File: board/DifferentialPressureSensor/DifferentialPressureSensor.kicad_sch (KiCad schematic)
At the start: 15 parts, among them U1 ESP32-S3-DEVKIT-LIPO

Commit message: -Enhance Datalogger Functionality and Update Rotary Encoder Configuration - Updated the datalogger_task to initialize sensor readings after resuming from sleep, ensuring fresh data is captured. - Changed the rotary encoder button pin from GPIO_NUM_7 to GPIO_NUM_2 - Adjusted inactivity timeout and sleep duration for better power management. - Added a callback for long button presses on the rotary encoder to enhance user interaction. - updated kicad design
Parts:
- R4: value 10k -> 4.7k
- R5: value 2k -> 4.7k
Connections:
- net +3.3V: now also Jrotary1.2 (Pin_2); no longer Jrotary1.1 (Pin_1)
- net GND: now also Jrotary1.1 (Pin_1); no longer Jrotary1.2 (Pin_2)
- net at U1.J3_2 (U0TXD/GPIO43): no longer Jrotary1.3 (Pin_3)
- net at U1.J3_5 (GPIO2): now also Jrotary1.3 (Pin_3)
- net at U1.J3_6 (GPIO42): now also Jrotary1.5 (Pin_5); no longer Jrotary1.4 (Pin_4)
- net at U1.J3_7 (GPIO41): now also Jrotary1.4 (Pin_4); no longer Jrotary1.5 (Pin_5)
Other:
- moved on the sheet: Ji2c1, Ji2c2, Ji2c3, Joled1, Jrotary1

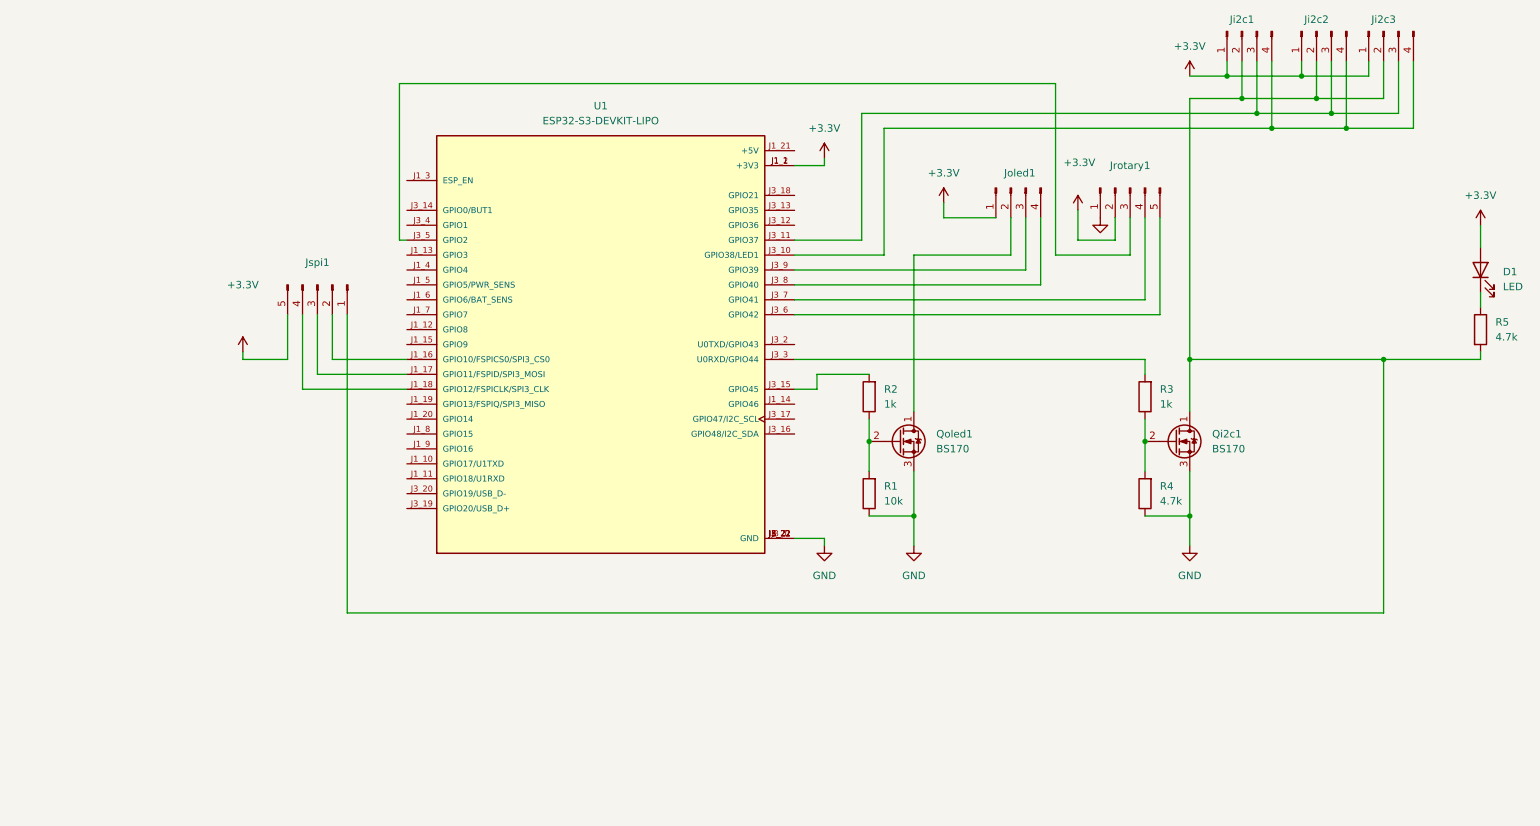
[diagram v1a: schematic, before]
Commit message: updated pins on sch file and completed routing of PCB, sucks bad, but holds togeter with 1 layer only :-D
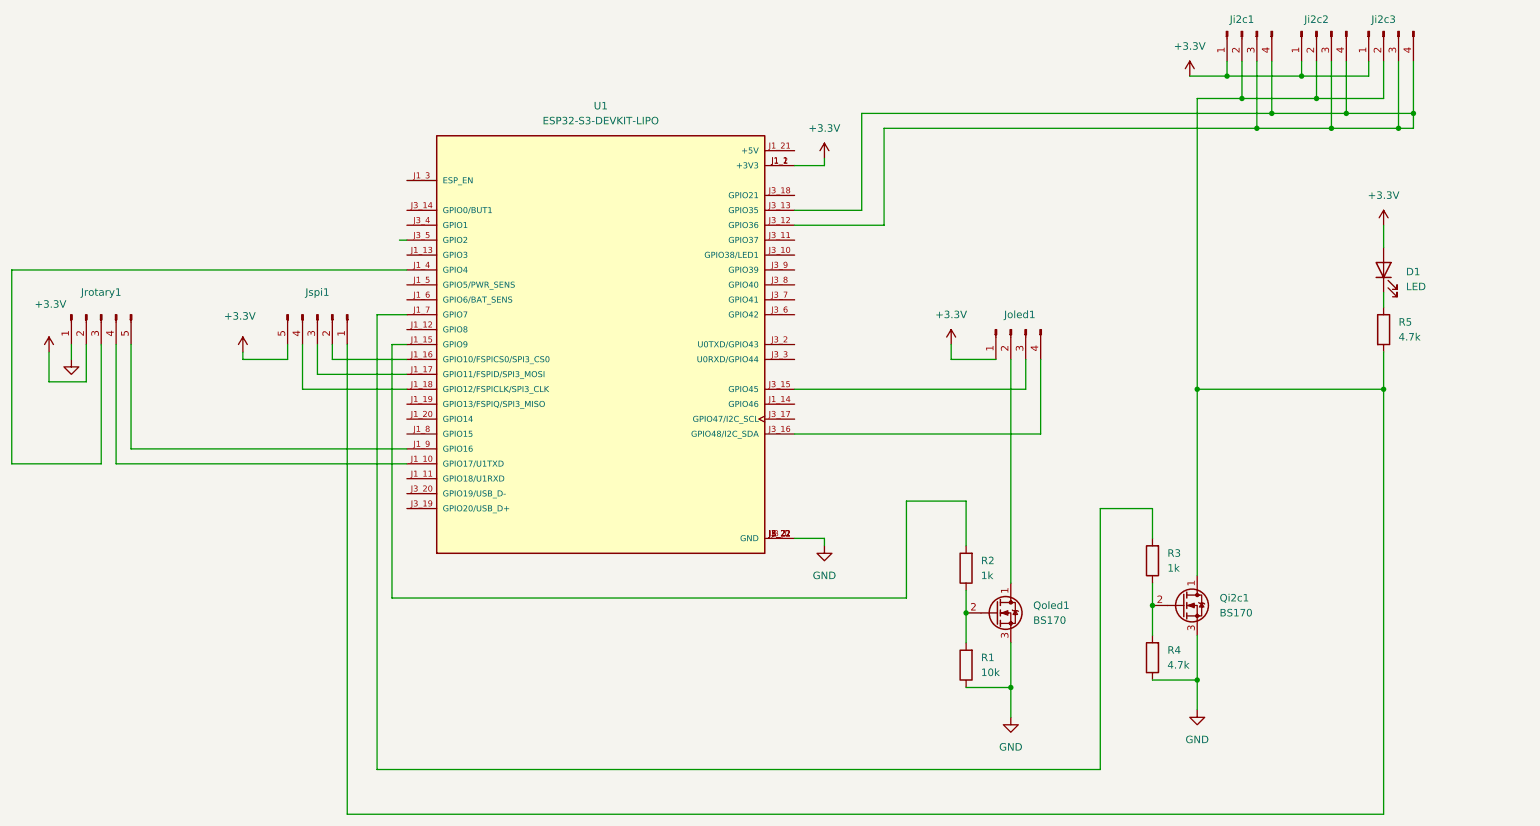
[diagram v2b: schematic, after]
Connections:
- net at Joled1.3 (Pin_3): now also U1.J3_15 (GPIO45); no longer U1.J3_9 (GPIO39)
- net at Joled1.4 (Pin_4): now also U1.J3_16 (GPIO48/I2C_SDA); no longer U1.J3_8 (GPIO40)
- net at R3.2: now also U1.J1_7 (GPIO7); no longer U1.J3_3 (U0RXD/GPIO44)
- net at U1.J1_10 (GPIO17/U1TXD): now also Jrotary1.4 (Pin_4)
- net at U1.J1_15 (GPIO9): now also R2.2
- net at U1.J1_4 (GPIO4): now also Jrotary1.3 (Pin_3)
- net at U1.J1_9 (GPIO16): now also Jrotary1.5 (Pin_5)
- net at Ji2c1.4 (Pin_4), Ji2c2.4 (Pin_4), Ji2c3.4 (Pin_4): now also Ji2c1.3 (Pin_3), Ji2c2.3 (Pin_3), Ji2c3.3 (Pin_3), U1.J3_12 (GPIO36), U1.J3_13 (GPIO35); no longer U1.J3_10 (GPIO38/LED1)
- net at U1.J3_5 (GPIO2): no longer Jrotary1.3 (Pin_3)
- net at U1.J3_6 (GPIO42): no longer Jrotary1.5 (Pin_5)
- net at U1.J3_7 (GPIO41): no longer Jrotary1.4 (Pin_4)
- now unconnected: U1.J3_11 (GPIO37)
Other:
- moved on the sheet: D1, Joled1, Jrotary1, Jspi1, Qi2c1, Qoled1, R1, R2, R3, R4, R5

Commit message: fixed error on schematic, applied auto routing, created components bom
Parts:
- R1: value 10k -> 4.7k
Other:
- title: (none) -> Differentia Pressure Sensor 
- moved on the sheet: D1, Ji2c1, Ji2c2, Ji2c3, R5

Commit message: doc
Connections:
- net at Ji2c1.3 (Pin_3), Ji2c2.3 (Pin_3), Ji2c3.3 (Pin_3)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: no longer Ji2c1.4 (Pin_4), Ji2c2.4 (Pin_4), Ji2c3.4 (Pin_4), U1.J3_13 (GPIO35)
- new net: Ji2c1.4 (Pin_4), Ji2c2.4 (Pin_4), Ji2c3.4 (Pin_4), U1.J3_13 (GPIO35)
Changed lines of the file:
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@@
-	)
-	(junction
-		(at 248.92 55.88)
-		(diameter 0)
-		(color 0 0 0 0)
 	)
 	(junction
@@
 		(color 0 0 0 0)
 	)
-	(junction
-		(at 246.38 58.42)
-		(diameter 0)
-		(color 0 0 0 0)
-	)
 	(wire
 		(pts
@@
 	(wire
 		(pts
-			(xy 248.92 55.88) (xy 248.92 58.42)
-		)
-		(stroke
-			(width 0)
-			(type default)
-		)
-	)
-	(wire
-		(pts
 			(xy 85.09 73.66) (xy 80.01 73.66)
 		)
@@
 		)
 		(stroke
-			(width 0)
-			(type default)
-		)
-	)
-	(wire
-		(pts
-			(xy 246.38 58.42) (xy 248.92 58.42)
-		)
-		(stroke
